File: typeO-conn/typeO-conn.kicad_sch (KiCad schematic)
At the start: 5 parts, among them J1 USB_C_Receptacle_USB2.0, J2 829-22-005-20-001101

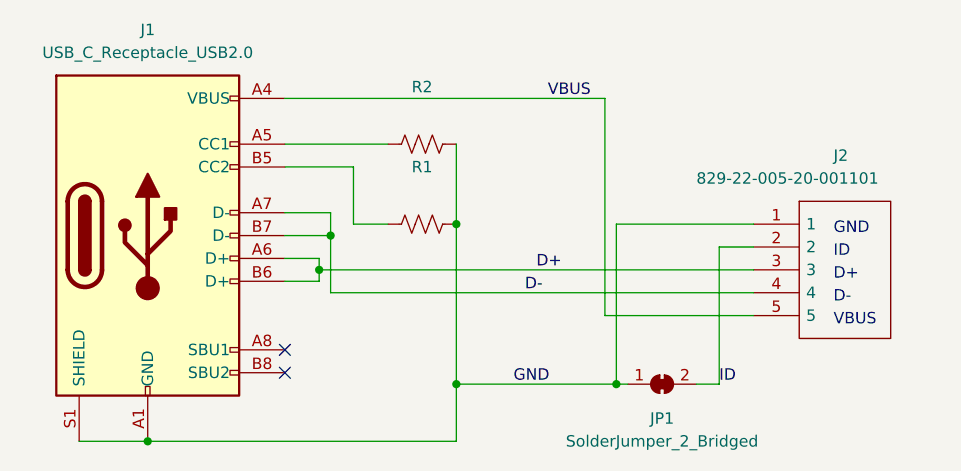
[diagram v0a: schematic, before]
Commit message: Rearrange and update silkscreen
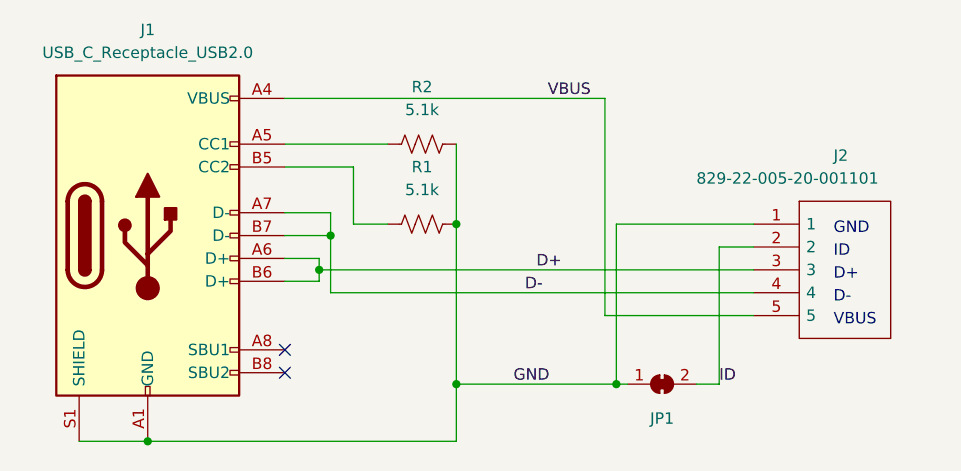
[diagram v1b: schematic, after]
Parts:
- JP1: value SolderJumper_2_Bridged -> (none); footprint Jumper:SolderJumper-2_P1.3mm_Open_TrianglePad1.0x1.5mm -> (none)
- R1, R2: value (none) -> 5.1k
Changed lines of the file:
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@@
     (in_bom yes) (on_board yes) (fields_autoplaced)
     (property "Reference" "R1" (id 0) (at 129.54 90.17 90))
-    (property "Value" "" (id 1) (at 129.54 92.71 90))
+    (property "Value" "5.1k" (id 1) (at 129.54 92.71 90))
     (property "Footprint" "Resistor_THT:R_Axial_DIN0207_L6.3mm_D2.5mm_P7.62mm_Horizontal" (id 2) (at 129.286 97.536 90)
       (effects (font (size 1.27 1.27)) hide)
@@
     (in_bom yes) (on_board yes)
     (property "Reference" "JP1" (id 0) (at 156.21 118.11 0))
-    (property "Value" "SolderJumper_2_Bridged" (id 1) (at 156.21 120.65 0))
-    (property "Footprint" "Jumper:SolderJumper-2_P1.3mm_Open_TrianglePad1.0x1.5mm" (id 2) (at 156.21 114.3 0)
+    (property "Value" "" (id 1) (at 156.21 120.65 0))
+    (property "Footprint" "" (id 2) (at 156.21 114.3 0)
       (effects (font (size 1.27 1.27)) hide)
     )
@@
     (in_bom yes) (on_board yes) (fields_autoplaced)
     (property "Reference" "R2" (id 0) (at 129.54 81.28 90))
-    (property "Value" "" (id 1) (at 129.54 83.82 90))
+    (property "Value" "5.1k" (id 1) (at 129.54 83.82 90))
     (property "Footprint" "Resistor_THT:R_Axial_DIN0207_L6.3mm_D2.5mm_P7.62mm_Horizontal" (id 2) (at 129.286 88.646 90)
       (effects (font (size 1.27 1.27)) hide)
@@
     )
     (path "/900a5489-bd90-4421-bdbf-8e442b205258"
-      (reference "JP1") (unit 1) (value "SolderJumper_2_Bridged") (footprint "Jumper:SolderJumper-2_P1.3mm_Open_TrianglePad1.0x1.5mm")
+      (reference "JP1") (unit 1) (value "SolderJumper_2_Bridged") (footprint "Jumper:SolderJumper-2_P1.3mm_Bridged_RoundedPad1.0x1.5mm")
     )
     (path "/7342cc82-e0e9-41f9-8b46-68197771b07f"
